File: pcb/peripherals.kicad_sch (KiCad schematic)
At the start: 12 parts, among them J10 SPI, J14 SERIAL, J3 INDICATOR, J8 QWIIC1, J9 QWIIC2, Q1 MMBT2222A

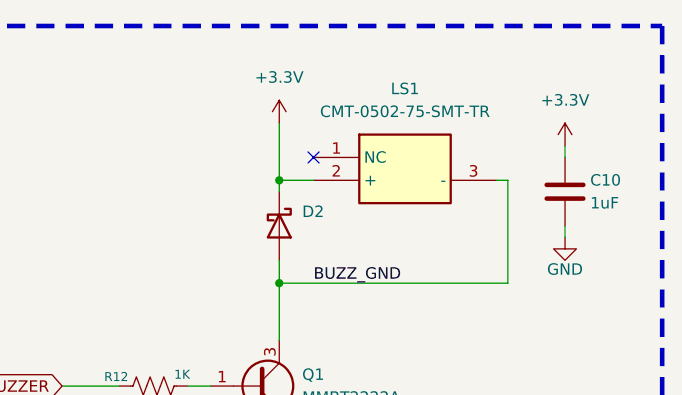
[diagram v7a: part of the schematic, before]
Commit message: Fixed cap values on reset button
Fixed all part numbers and extended parameters.
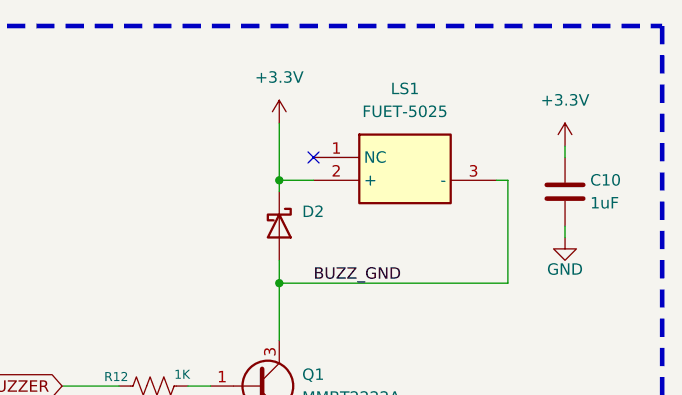
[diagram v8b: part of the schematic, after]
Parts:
- C10: Digikey (none) -> 1276-1019-2-ND; LCSC_PN C6119849 -> (none); MF HRE -> (none); Mouser (none) -> 187-CL10B105KO8NNNC
- D2: Digikey (none) -> 1727-5834-2-ND; MN (none) -> Shikues; Mouser (none) -> 771-PMEG3010EB115
- D21, D22: LCSC_PN C5563754 -> (none); MF FUXINSEMI -> (none)
- J10: LCSC_PN C2919601 -> (none); MF JST -> (none)
- J14, J3: Digikey (none) -> 455-BM03B-SRSS-TBTR-ND; LCSC_PN C2919600 -> (none); MF JST -> (none); Mouser (none) -> 306-3BSRSSTBTLP
- J8, J9: Digikey (none) -> 455-BM04B-SRSS-TBTR-ND; LCSC_PN C2919601 -> (none); MF JST -> (none); Mouser (none) -> 306-BM04BSRSSTBTLFSN
- LS1: value CMT-0502-75-SMT-TR -> FUET-5025; Digikey (none) -> 102-CMT-0502-75-SMT-TR-ND; MF Same Sky -> (none); MN Same Sky -> Fuet; MPN CMT-0502-75-SMT-TR -> FUET-5025
- Q1: Digikey (none) -> MMBT2222AT-FDITR-ND; MF Diodes Incorporated -> (none)
- R12: Digikey (none) -> CR0603-JW-102ELFTR-ND; LCSC_PN C2907113 -> (none); MF FOJAN -> (none); Mouser (none) -> 652-CR0603-JW-102ELF
